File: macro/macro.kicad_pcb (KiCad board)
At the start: 2 copper layers, 81 x 23.8 mm, 4 parts, among them SW3 SW_Push, SW6 SW_Push, SW8 SW_Push, U2 XIAO-RP2040-DIP

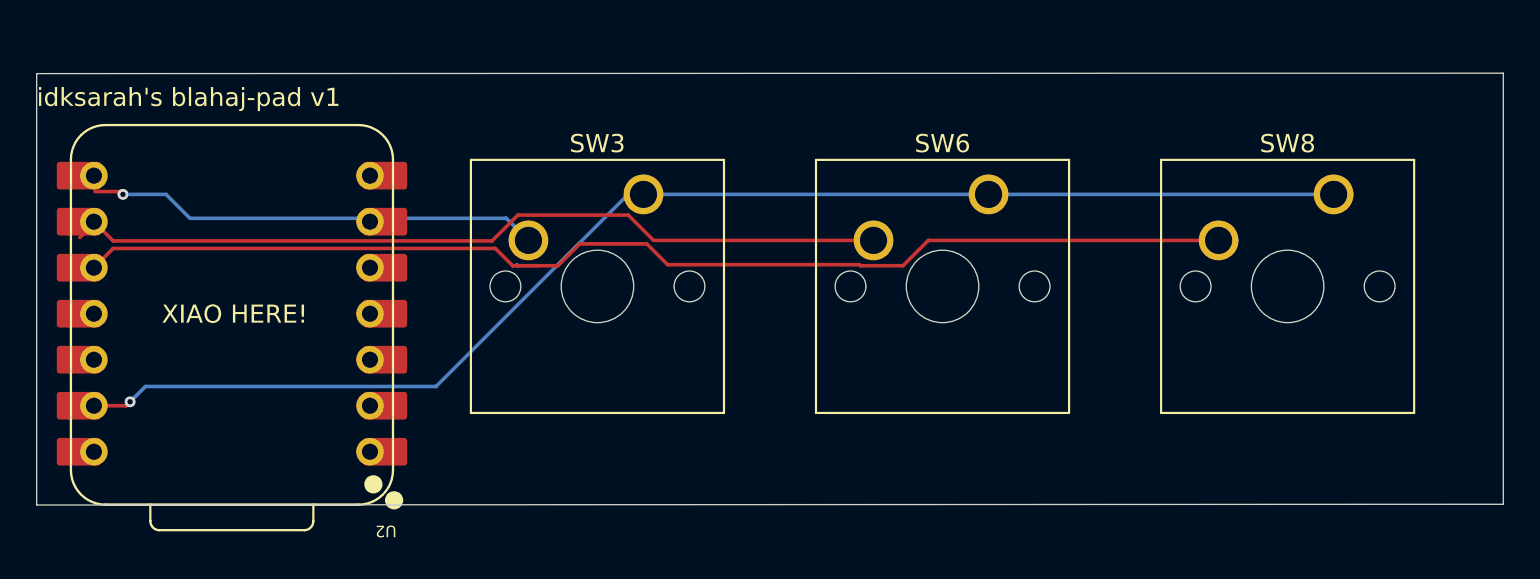
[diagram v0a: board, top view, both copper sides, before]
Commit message: usb port front -> back
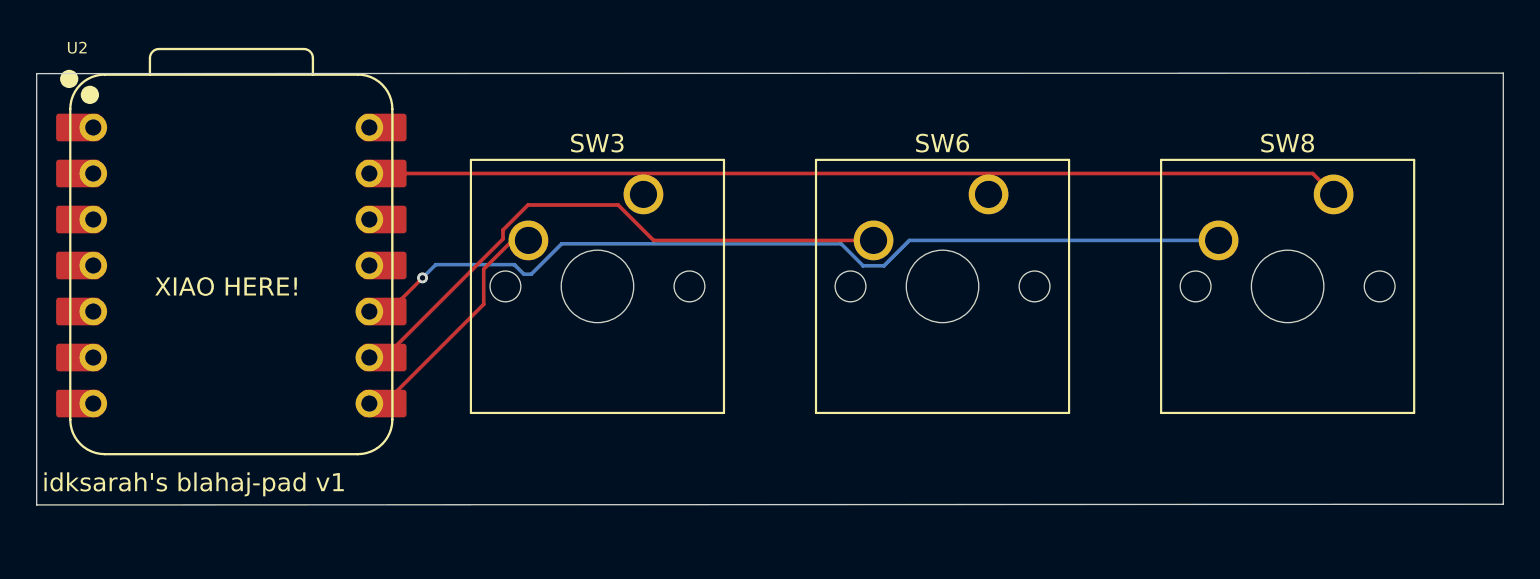
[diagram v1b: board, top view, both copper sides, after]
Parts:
- moved U2 2.66 mm to (86.9, 106.3), turned to 0 degrees
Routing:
- net GND: track 73.3 -> 52.9 mm, vias 1 -> 0
- net Net-(U2-GPIO2/SCK): track 46.4 -> 31.6 mm
- net Net-(U2-GPIO4/MISO): track 64.5 -> 49.9 mm, vias 0 -> 1
- net Net-(U2-GPIO1/RX): track 25.0 -> 12.8 mm, vias 1 -> 0
- net unconnected-(U2-GPIO28/ADC2/A2-Pad3): track 1.24 -> 0.00 mm
